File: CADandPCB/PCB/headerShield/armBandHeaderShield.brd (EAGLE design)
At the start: 22.9 x 59.7 mm, 11 parts

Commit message: Offset swtich headers.
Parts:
- removed SWITCH_HEADERS: 455-1750-1-ND, SparkFun-Connectors:1X03
- added J4, J5, J6: (no value), SparkFun-Connectors:1X01
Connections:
- net N$1: now also J5.1; no longer SWITCH_HEADERS.2
- net VIN: now also J6.1; no longer SWITCH_HEADERS.1
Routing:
- net N$1: track 19.6 -> 17.5 mm
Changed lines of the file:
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@@
 <text x="19.05" y="4.191" size="0.6096" layer="25" font="vector" ratio="20" align="bottom-center">D13</text>
 <text x="3.81" y="43.561" size="0.6096" layer="25" font="vector" ratio="20" align="bottom-center">TX</text>
-<text x="16.383" y="58.166" size="0.6096" layer="25" font="vector" ratio="20" align="bottom-center">OFF             ON</text>
+<text x="16.383" y="57.531" size="0.6096" layer="25" font="vector" ratio="20" align="bottom-center">OFF             ON</text>
 </plain>
 <attributes>
@@
 <attribute name="VALUE" x="2.413" y="53.213" size="0.6096" layer="27" font="vector" ratio="20"/>
 </element>
-<element name="SWITCH_HEADERS" library="SparkFun-Connectors" package="1X03" value="455-1750-1-ND" x="19.05" y="55.88" smashed="yes" rot="R180">
-<attribute name="PROD_ID" value="XXX-00000" x="19.05" y="55.88" size="1.778" layer="27" rot="R180" display="off"/>
-</element>
 <element name="J1" library="SparkFun-Connectors" package="1X04" value="" x="7.239" y="36.83" smashed="yes">
 <attribute name="PROD_ID" value="CONN-09696" x="7.239" y="36.83" size="1.778" layer="27" display="off"/>
@@
 <element name="FROM_TX" library="SparkFun-Connectors" package="1X01" value="" x="3.81" y="48.26" smashed="yes">
 <attribute name="VALUE" x="2.54" y="46.736" size="0.6096" layer="27" font="vector" ratio="20" align="top-left"/>
+</element>
+<element name="J4" library="SparkFun-Connectors" package="1X01" value="" x="13.97" y="55.753" smashed="yes">
+<attribute name="VALUE" x="12.7" y="54.229" size="0.6096" layer="27" font="vector" ratio="20" align="top-left"/>
+</element>
+<element name="J5" library="SparkFun-Connectors" package="1X01" value="" x="16.51" y="57.531" smashed="yes">
+<attribute name="VALUE" x="15.24" y="56.007" size="0.6096" layer="27" font="vector" ratio="20" align="top-left"/>
+</element>
+<element name="J6" library="SparkFun-Connectors" package="1X01" value="" x="19.05" y="55.753" smashed="yes">
+<attribute name="VALUE" x="17.78" y="54.229" size="0.6096" layer="27" font="vector" ratio="20" align="top-left"/>
 </element>
 </elements>
@@
 <signal name="VIN">
 <contactref element="RIGHT_HEADER" pad="15"/>
-<contactref element="SWITCH_HEADERS" pad="1"/>
-<wire x1="19.05" y1="55.88" x2="19.05" y2="41.91" width="0.508" layer="1"/>
+<contactref element="J6" pad="1"/>
+<wire x1="19.05" y1="55.753" x2="19.05" y2="41.91" width="0.508" layer="1"/>
 </signal>
 <signal name="N$7">
@@
 <signal name="N$1">
 <contactref element="VIN_HEADERS" pad="1"/>
-<contactref element="SWITCH_HEADERS" pad="2"/>
-<wire x1="12.7" y1="58.293" x2="15.367" y2="58.293" width="0.508" layer="1"/>
-<wire x1="16.51" y1="55.88" x2="16.51" y2="57.15" width="0.508" layer="1"/>
-<wire x1="16.51" y1="57.15" x2="15.367" y2="58.293" width="0.508" layer="1"/>
+<wire x1="11.938" y1="57.531" x2="16.51" y2="57.531" width="0.508" layer="1"/>
 <wire x1="3.81" y1="55.88" x2="3.81" y2="53.34" width="0.508" layer="1"/>
 <wire x1="3.81" y1="53.34" x2="4.445" y2="52.705" width="0.508" layer="1"/>
 <wire x1="4.445" y1="52.705" x2="7.112" y2="52.705" width="0.508" layer="1"/>
-<wire x1="7.112" y1="52.705" x2="12.7" y2="58.293" width="0.508" layer="1"/>
+<wire x1="7.112" y1="52.705" x2="11.938" y2="57.531" width="0.508" layer="1"/>
+<contactref element="J5" pad="1"/>
 </signal>
 <signal name="A0">

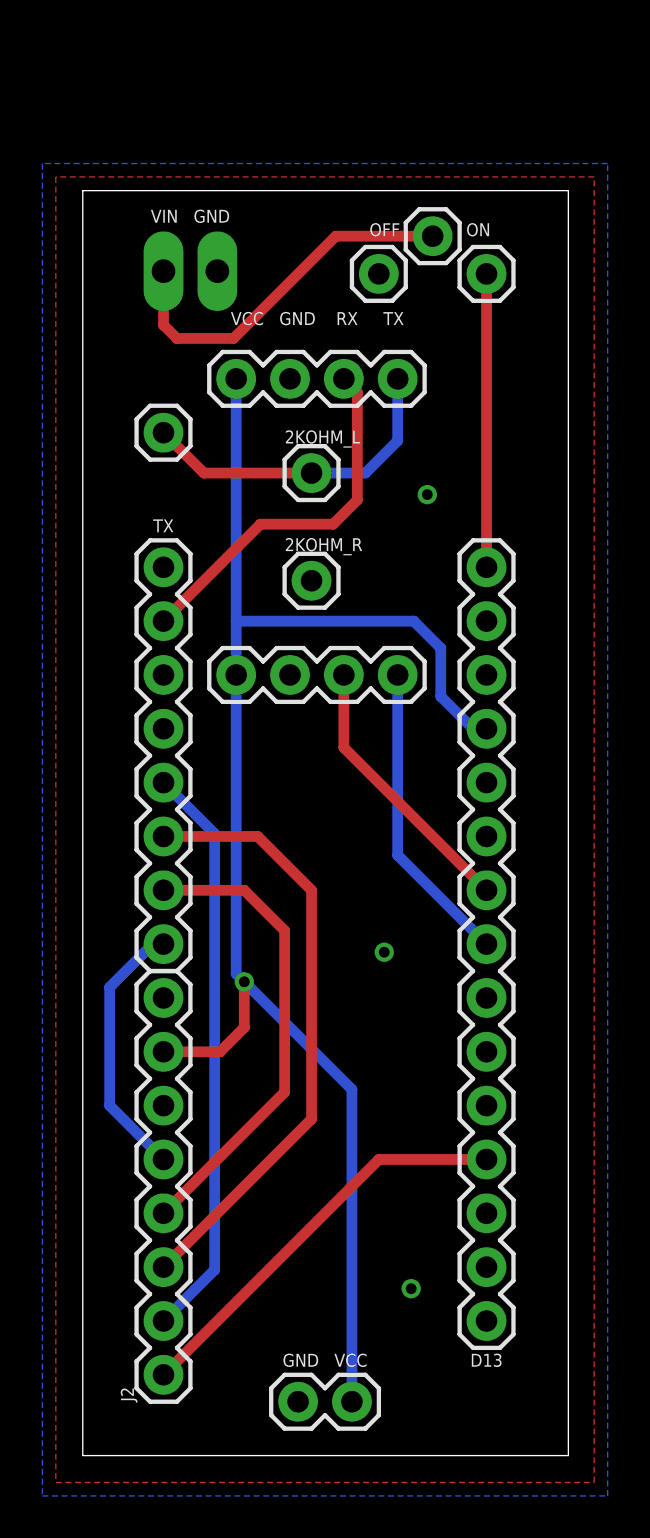
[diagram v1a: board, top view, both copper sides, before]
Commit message: Commit Gerber files and final rev 1 for the header version of board.
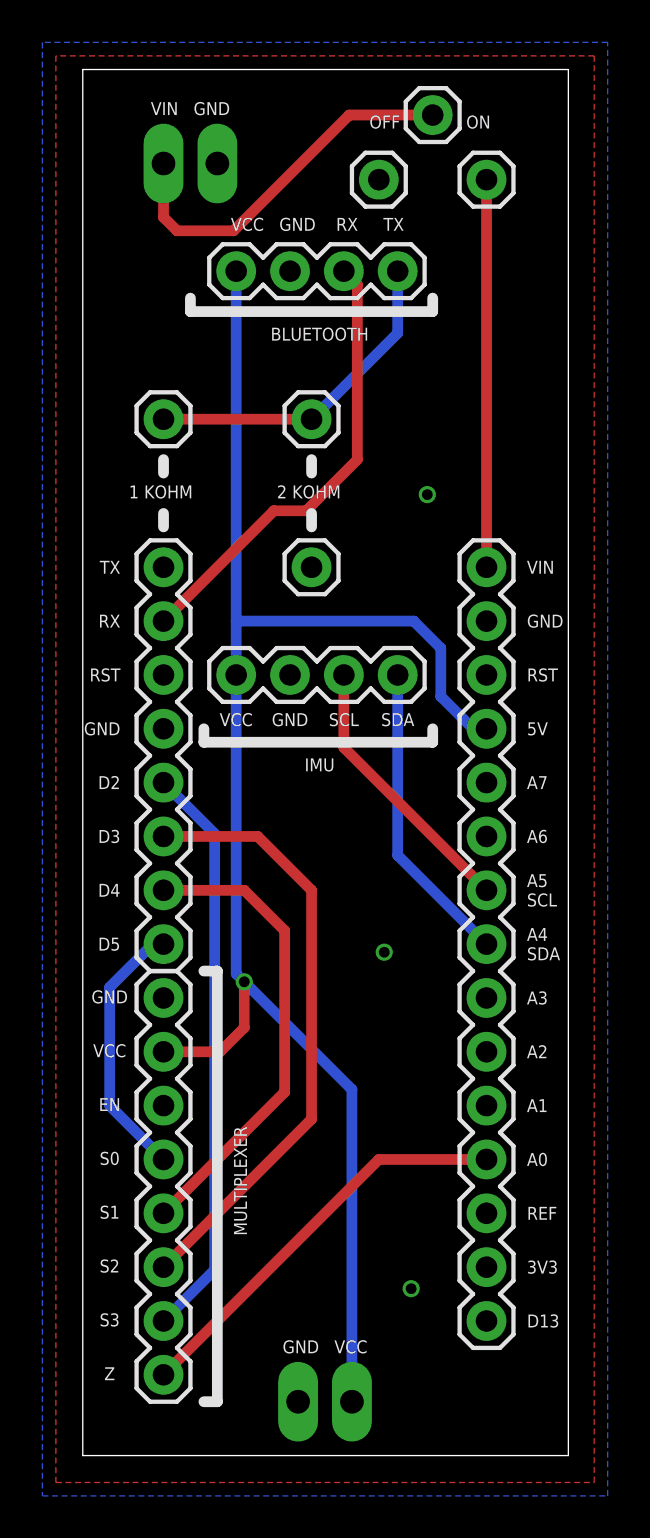
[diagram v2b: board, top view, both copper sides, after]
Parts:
- removed VCC_HEADERS: (no value), SparkFun-Connectors:1X02
- added VCC_OUT: (no value), SparkFun-Connectors:1X02_LONGPADS
- moved J5 5.72 mm to (16.5, 63.2)
- moved BT_HEADERS 5.08 mm to (7.24, 55.9)
- moved VIN_HEADERS 5.08 mm to (3.81, 61.0)
- moved J4 4.45 mm to (14.0, 60.2)
- moved J6 4.45 mm to (19.1, 60.2)
- moved 2KOHM_L 2.54 mm to (10.8, 48.9)
- moved FROM_TX 0.64 mm to (3.81, 48.9)
- moved 2KOHM_R 0.63 mm to (10.8, 41.9)
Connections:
- net GND: now also VCC_OUT.1; no longer VCC_HEADERS.1
- net VCC: now also VCC_OUT.2; no longer VCC_HEADERS.2
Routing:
- net VCC: track 72.2 -> 77.3 mm
- net VIN: track 13.8 -> 18.3 mm
- net RX: track 17.5 -> 21.5 mm
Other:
- board size 22.9 x 59.7 mm -> 22.9 x 65.4 mm
- board text added: "1 KOHM"
- board text added: "2 KOHM"
- board text added: "3V3"
- board text added: "5V"
- board text added: "A0"
- board text added: "A1"
- board text added: "A2"
- board text added: "A3"
- board text added: "A4 SDA"
- board text added: "A5 SCL"
- board text added: "A6"
- board text added: "A7"
- board text added: "BLUETOOTH"
- board text added: "D2"
- board text added: "D3"
- board text added: "D4"
- board text added: "D5"
- board text added: "EN"
- board text added: "GND"
- board text added: "IMU"
- board text added: "MULTIPLEXER"
- board text added: "REF"
- board text added: "RST"
- board text added: "RX"
- board text added: "S0"
- board text added: "S1"
- board text added: "S2"
- board text added: "S3"
- board text added: "SCL"
- board text added: "SDA"
- board text added: "VCC"
- board text added: "VIN"
- board text added: "Z"
